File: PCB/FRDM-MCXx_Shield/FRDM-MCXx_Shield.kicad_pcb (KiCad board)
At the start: 2 copper layers, 91.4 x 54.6 mm, 45 parts, among them J1 Conn_01x05_Socket, J3 Conn_01x04_Socket, M1 Motor_Servo, SW1 PEC11L-4120F-N0020, SW2 SW_Push, U1 STPIC6C595MTR, U2 SN74LV164ADR, U3 M95010-RMN6TP, U4 FXLS8974CF, U5 SHT31A-DIS

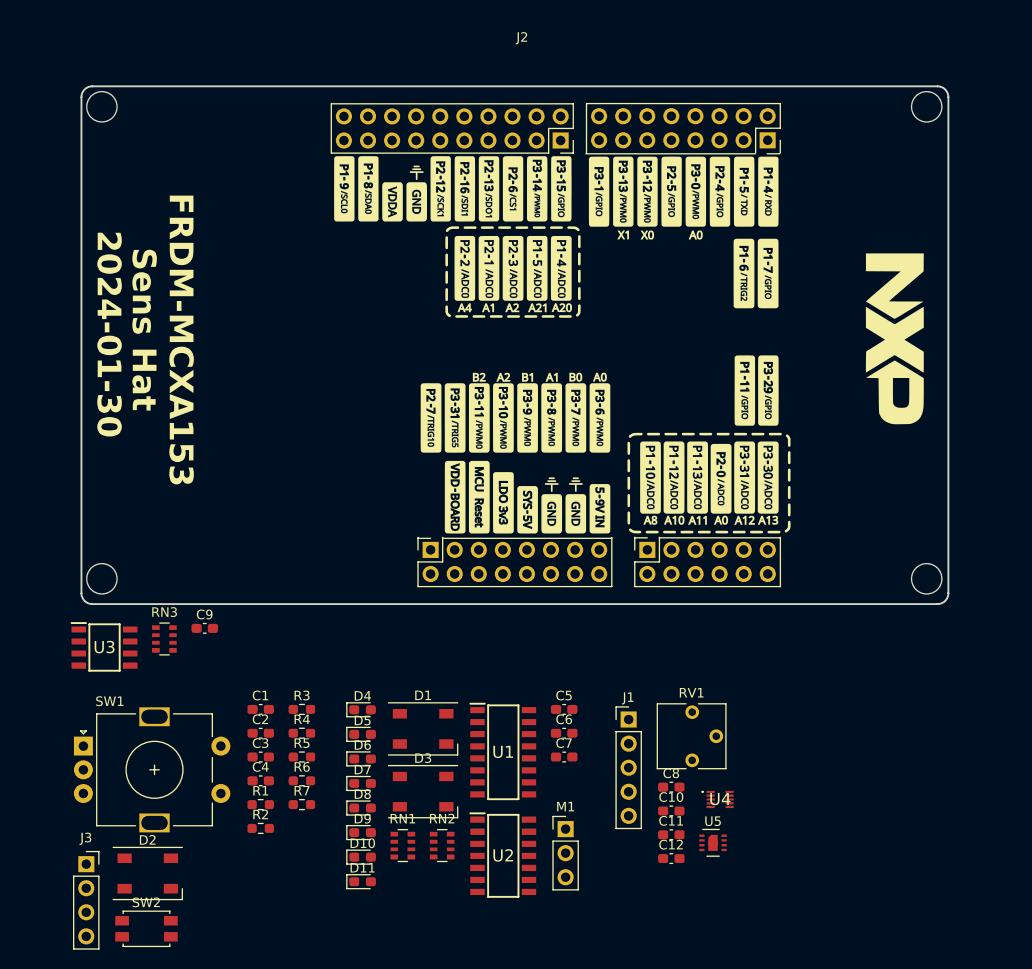
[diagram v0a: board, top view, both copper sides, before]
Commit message: Update schematic and footprint
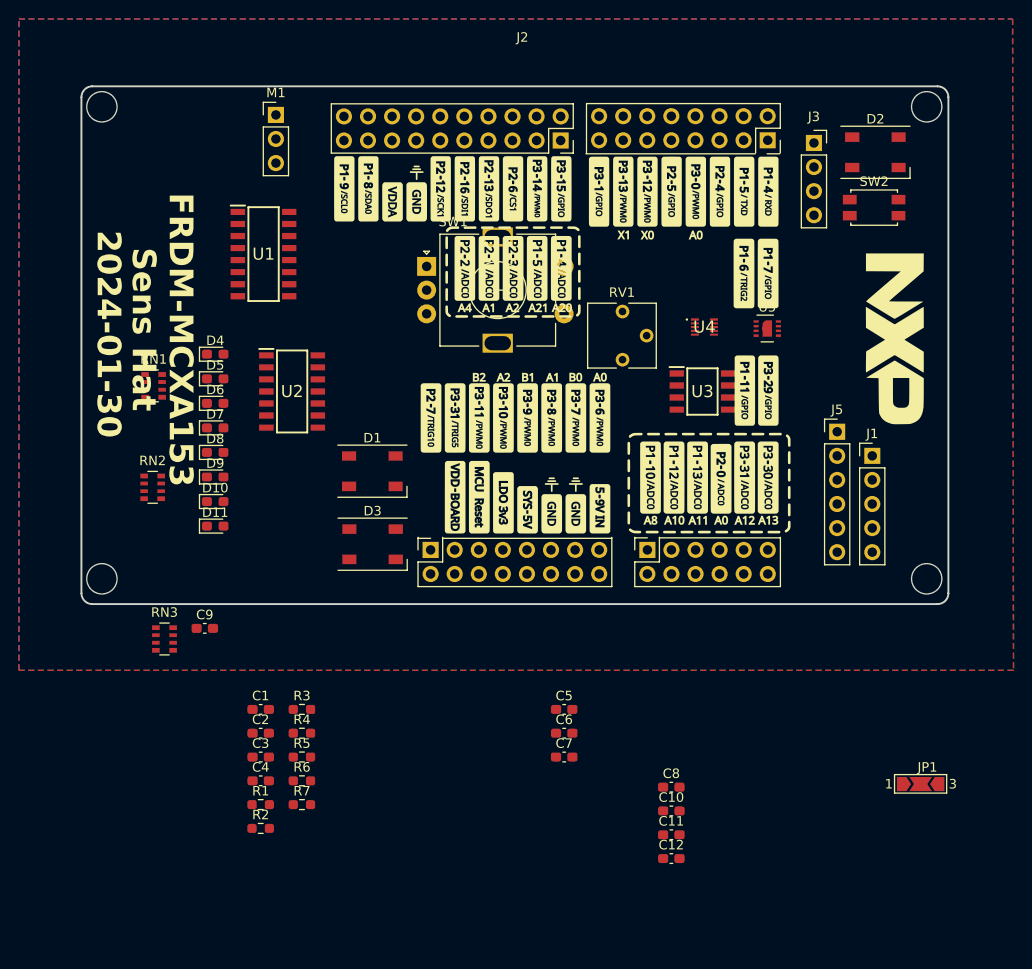
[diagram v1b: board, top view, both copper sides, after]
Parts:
- added J5: Conn_01x06_Socket, Connector_PinHeader_2.54mm:PinHeader_1x06_P2.54mm_Vertical, F.Cu at (183.9, 95.5)
- added JP1: SolderJumper_3_Open, Jumper:SolderJumper-3_P2.0mm_Open_TrianglePad1.0x1.5mm_NumberLabels, F.Cu at (192.7, 132.7)
- moved D2 108.1 mm to (187.9, 66.1)
- moved SW2 108.1 mm to (187.8, 71.9)
- moved J3 108.1 mm to (181.4, 65.1)
- moved M1 81.3 mm to (124.7, 62.1)
- moved U3 68.6 mm to (169.7, 91.3)
- moved SW1 62.2 mm to (140.6, 78.1)
- moved U1 58.3 mm to (123.4, 76.8)
- moved RN1 55.2 mm to (111.8, 90.7)
- moved U5 54.5 mm to (176.5, 84.7)
- moved U2 53.8 mm to (126.4, 91.3)
- moved U4 49.8 mm to (169.9, 84.5)
- moved RN2 48.6 mm to (111.7, 101.4)
- moved RV1 42.9 mm to (161.3, 87.9)
- moved D11 40.6 mm to (118.3, 105.5)
- moved D10 40.6 mm to (118.3, 102.9)
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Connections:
- net /Actuators/LED_NEOPIXEL renamed /LED_NEOPIXEL
- net /Actuators/~{SPI_CS} renamed /~{SPI_CS}
- net /HMI/ENC_SW renamed /ENC_SW
- net /HMI/LED_B renamed /LED_B
- net /HMI/LED_G renamed /LED_G
- net /HMI/LED_R renamed /LED_R
- net /Sensors/ACEL_INT1 renamed /ACEL_INT1
- net /Sensors/GPS_PPS renamed /GPS_PPS
- C8 pad 1: +3.3V -> Net-(JP1-C)
- J1 pad 3: /Sensors/GPS_TX -> /RX
- J1 pad 4: /Sensors/GPS_RX -> /TX
- J2 pad 1: unconnected-(J2-Pad1) -> /ENC_B
- J2 pad 10: unconnected-(J2A-SYS-5V-Pad10) -> +5V
- J2 pad 12: unconnected-(J2A-GND-Pad12) -> /ACEL_INT2
- J2 pad 14: unconnected-(J2A-GND-Pad14) -> /SERVO_PWM
- J2 pad 16: unconnected-(J2A-5-9VIN-Pad16) -> +3.3VADC
- J2 pad 18: unconnected-(J2B-P1-8/SDA0-Pad18) -> /SDA
- J2 pad 2: unconnected-(J2A-NC-Pad2) -> /ADC_OUT
- J2 pad 20: unconnected-(J2B-P1-9/SCL0-Pad20) -> /SCL
- J2 pad 3: unconnected-(J2-Pad3) -> /ENC_A
- J2 pad 4: unconnected-(J2A-VDD-BOARD-Pad4) -> +3.3V
- J2 pad 5: unconnected-(J2-Pad5) -> /SWITCH
- J2 pad 6: unconnected-(J2A-MCU-RESETb-Pad6) -> /ACEL_CS
- J2 pad 7: unconnected-(J2-Pad7) -> /~{TEMP_RST}
- J2 pad 8: unconnected-(J2A-LDO-3v3-Pad8) -> +3.3V
- J2 pad 9: unconnected-(J2-Pad9) -> /TEMP_ALERT
- J3 pad 1: /HMI/SDA -> /SDA
- J3 pad 2: /HMI/SCL -> /SCL
- M1 pad 1: /Actuators/SERVO_PWM -> /SERVO_PWM
- R1 pad 2: /HMI/SWITCH -> /SWITCH
- R3 pad 2: /HMI/ENC_A -> /ENC_A
- R4 pad 2: /HMI/ENC_B -> /ENC_B
- RN3 pad 2: /Sensors/ACEL_INT2 -> /ACEL_INT2
- RV1 pad 1: +3.3V -> Net-(JP1-C)
- RV1 pad 2: /Sensors/ADC_OUT -> /ADC_OUT
- U2 pad 1: /Actuators/SPI_MOSI -> /SPI_MOSI
- U2 pad 2: /Actuators/SPI_MOSI -> /SPI_MOSI
- U2 pad 8: /Actuators/SPI_CLK -> /SPI_CLK
- U4 pad 3: /Sensors/SPI_MISO -> /SPI_MISO
- U4 pad 4: /Sensors/SPI_MOSI -> /SPI_MOSI
- U4 pad 5: /Sensors/SPI_CLK -> /SPI_CLK
- U4 pad 6: /Sensors/ACEL_INT2 -> /ACEL_INT2
- U4 pad 7: /Sensors/ACEL_CS -> /ACEL_CS
- U5 pad 1: /Sensors/SDA -> /SCL
- U5 pad 3: /Sensors/TEMP_ALERT -> /TEMP_ALERT
- U5 pad 4: /Sensors/SCL -> /SDA
- U5 pad 6: /Sensors/~{TEMP_RST} -> /~{TEMP_RST}
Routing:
- added copper zone on B.Cu, net GND
- added copper zone on F.Cu, net GND

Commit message: Updated schematic and PCB
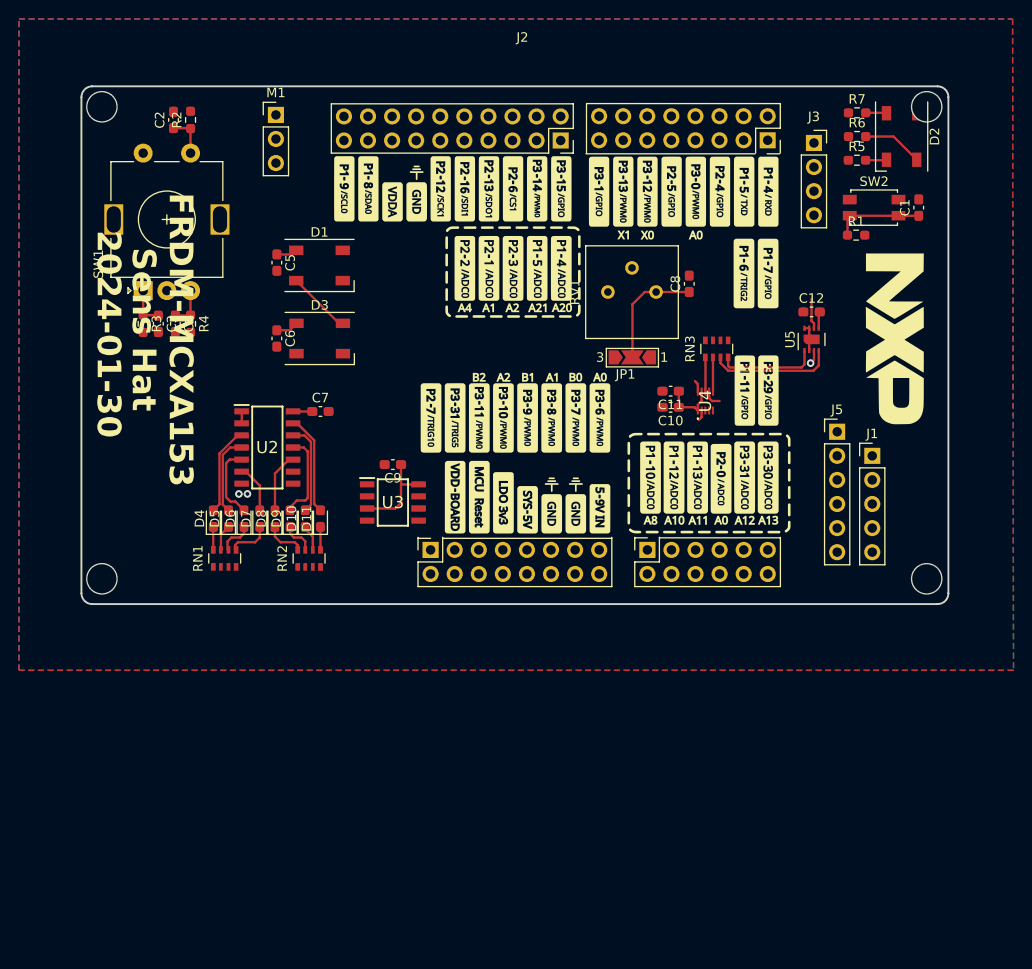
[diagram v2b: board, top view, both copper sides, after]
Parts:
- removed U1: STPIC6C595MTR, SamacSys_Parts:SOIC127P600X175-16N
- RV1: footprint Potentiometer_THT:Potentiometer_Vishay_T73YP_Vertical -> Potentiometer_THT:Potentiometer_Bourns_3386P_Vertical
- moved R7 93.6 mm to (186.0, 61.9)
- moved R6 89.7 mm to (186.0, 64.4)
- moved C1 87.3 mm to (192.5, 71.9), turned to 90 degrees
- moved R1 86.9 mm to (185.9, 74.8)
- moved R5 86.0 mm to (186.0, 66.9)
- moved R2 75.1 mm to (115.7, 62.6), turned to 90 degrees
- moved RN3 65.8 mm to (171.2, 86.8), turned to 90 degrees
- moved C2 65.3 mm to (113.9, 62.6), turned to 90 degrees
- moved C12 59.5 mm to (181.2, 82.9)
- moved C5 56.0 mm to (124.8, 77.7), turned to -90 degrees
- moved JP1 54.3 mm to (162.3, 87.7), turned to 180 degrees
- moved C8 53.1 mm to (168.3, 79.9), turned to 90 degrees
- moved C6 51.5 mm to (124.8, 85.7), turned to -90 degrees
- moved C4 49.0 mm to (114.1, 84.2), turned to -90 degrees
- moved C3 47.0 mm to (112.3, 84.2), turned to -90 degrees
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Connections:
- RN3 pad 3: /SCL -> /SDA
- RN3 pad 4: /SDA -> /SCL
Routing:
- net +3.3V: track 0.00 -> 24.3 mm
- net /SDA: track 0.00 -> 13.1 mm
- net Net-(JP1-C): track 0.00 -> 12.1 mm
- net /Actuators/LED_H: track 0.00 -> 10.6 mm
- net /SCL: track 0.00 -> 10.6 mm
- net /Actuators/LED_G: track 0.00 -> 9.64 mm
- net Net-(C1-Pad1): track 0.00 -> 9.43 mm
- net /Actuators/LED_A: track 0.00 -> 9.39 mm
- net /Actuators/LED_F: track 0.00 -> 9.22 mm
- net /Actuators/LED_B: track 0.00 -> 8.41 mm
- net /Actuators/LED_C: track 0.00 -> 7.85 mm
- net Net-(D1-DOUT): track 0.00 -> 6.79 mm
- net /Actuators/LED_E: track 0.00 -> 6.40 mm
- net Net-(D2-GK): track 0.00 -> 6.40 mm
- net GND: track 0.00 -> 5.41 mm, vias 0 -> 2
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
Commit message: Updated schematic and PCB files
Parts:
- added D1: RED, LED_SMD:LED_0603_1608Metric_Pad1.05x0.95mm_HandSolder, F.Cu at (164.5, 92.5)
- added D2: GREEN, LED_SMD:LED_0603_1608Metric_Pad1.05x0.95mm_HandSolder, F.Cu at (164.5, 94.4)
- added D3: BZV55B9V1, Diode_SMD:D_SOD-128, F.Cu at (108.3, 92.2)
- added F1: 300mA, Fuse:Fuse_0603_1608Metric_Pad1.05x0.95mm_HandSolder, F.Cu at (116.2, 93.0)
- added H1: MountingHole, MountingHole:MountingHole_2.5mm, F.Cu at (192.3, 103.1)
- added J2: Barrel_Jack_Switch, Connector_BarrelJack:BarrelJack_Wuerth_6941xx301002, F.Cu at (114.5, 100.7)
- added Q1: IRLML6401, Package_TO_SOT_SMD:SOT-23, F.Cu at (112.5, 92.2)
- added R1: 330, Resistor_SMD:R_0603_1608Metric_Pad0.98x0.95mm_HandSolder, F.Cu at (167.9, 92.5)
- added R2: 470, Resistor_SMD:R_0603_1608Metric_Pad0.98x0.95mm_HandSolder, F.Cu at (167.9, 94.4)
- added R3: 100k, Resistor_SMD:R_0603_1608Metric_Pad0.98x0.95mm_HandSolder, F.Cu at (112.5, 89.0)
- J4: renamed from J1; footprint Connector_PinHeader_2.54mm:PinHeader_1x05_P2.54mm_Vertical -> Connector_PinSocket_2.54mm:PinSocket_1x05_P2.54mm_Vertical
- J5: footprint Connector_PinHeader_2.54mm:PinHeader_1x06_P2.54mm_Vertical -> Connector_PinSocket_2.54mm:PinSocket_1x06_P2.54mm_Vertical
- moved C9 38.9 mm to (142.4, 86.2), turned to 90 degrees
- moved U3 35.9 mm to (145.3, 86.2), turned to 180 degrees
- moved C6 32.9 mm to (135.3, 80.2)
- moved C7 32.9 mm to (135.3, 81.9)
- moved RN1 32.9 mm to (140.2, 75.7)
- moved U2 32.9 mm to (139.0, 81.2)
- moved J3 24.5 mm to (183.3, 89.5), turned to 180 degrees
- moved C8 13.4 mm to (156.0, 85.3), turned to -90 degrees
- moved JP1 10.2 mm to (162.0, 77.5), turned to 0 degrees
- moved RV1 6.45 mm to (159.5, 84.4), turned to -90 degrees
- moved R7 4.04 mm to (181.9, 75.3)
- moved R10 4.04 mm to (182.0, 62.4)
- moved C5 4.04 mm to (188.5, 72.4)
- moved D4 4.04 mm to (186.7, 64.9)
- moved R8 4.04 mm to (182.0, 67.4)
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- renumbered C9 to C1, C5 to C10, C6 to C11, C7 to C12, C1 to C5, C11 to C6, C10 to C7, C12 to C9, D7 to D10, D8 to D11, D9 to D12, D10 to D13, D11 to D14, D2 to D4, D1 to D5, D3 to D6, D4 to D7, D5 to D8, D6 to D9, J2 to J1, R7 to R10, R2 to R4, R3 to R5, R4 to R6, R1 to R7, R5 to R8, R6 to R9, RN3 to RN1, RN1 to RN2, RN2 to RN3, U3 to U1, U4 to U2, U5 to U3, U2 to U5
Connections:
- JP1 pad 1: +3.3V -> +3.3VADC
- JP1 pad 3: +3.3VADC -> +3.3V
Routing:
- net +3.3V: track 24.3 -> 316.2 mm, vias 0 -> 11
- net +5V: track 0.00 -> 148.5 mm, vias 0 -> 2
- net /SPI_MOSI: track 1.27 -> 109.5 mm, vias 0 -> 3
- net /SPI_CLK: track 0.00 -> 82.6 mm, vias 0 -> 5
- net /SCL: track 10.6 -> 87.0 mm, vias 0 -> 2
- net /~{SPI_CS}: track 0.00 -> 72.1 mm, vias 0 -> 2
- net VBUS: track 0.00 -> 71.0 mm, vias 0 -> 1
- net /SWITCH: track 0.00 -> 70.2 mm, vias 0 -> 1
- net /SDA: track 13.1 -> 82.4 mm, vias 0 -> 1
- net /~{EEPROM_CS}: track 0.00 -> 62.6 mm, vias 0 -> 3
- net /ENC_SW: track 0.00 -> 62.2 mm, vias 0 -> 1
- net /ACEL_INT2: track 3.60 -> 63.5 mm, vias 0 -> 1
- net /ACEL_INT1: track 3.60 -> 62.5 mm, vias 0 -> 1
- net /SPI_MISO: track 0.00 -> 57.1 mm, vias 0 -> 2
- net /ENC_A: track 0.00 -> 54.7 mm
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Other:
- copper layers 2 -> 4

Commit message: Updated PCB
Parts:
- added ?: , clipboard:5e83e988-b69c-43c0-b382-9b895c3e7185, F.Cu at (187.2, 91.1)
- added Brd1: SSD1306, OLED:128x64OLED, F.Cu at (182.7, 85.5)
- moved R7 11.4 mm to (189.8, 67.1), turned to -90 degrees
- moved J3 10.0 mm to (193.3, 89.5)
- moved SW2 9.54 mm to (192.7, 69.0), turned to -90 degrees
- moved R8 5.36 mm to (182.3, 62.1), turned to -90 degrees
- moved R10 5.31 mm to (187.3, 62.1), turned to -90 degrees
- moved C5 4.39 mm to (192.7, 73.7), turned to 0 degrees
- moved R9 3.99 mm to (184.8, 62.1), turned to -90 degrees
- moved D4 2.66 mm to (184.8, 66.8), turned to 180 degrees
- moved J4 2.26 mm to (183.9, 100.3)
- moved J5 2.26 mm to (187.6, 97.8)
- moved M1 0.18 mm to (124.7, 62.3)
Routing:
- net +5V: track 148.5 -> 169.1 mm
- net /SDA: track 82.4 -> 95.6 mm
- net /SWITCH: track 70.2 -> 82.7 mm
- net /SCL: track 87.0 -> 99.4 mm
- net /LED_B: track 17.5 -> 23.7 mm
- net /LED_R: track 16.3 -> 12.6 mm
- net /TX: track 54.4 -> 56.7 mm
- net /RX: track 51.7 -> 53.9 mm
- net /GPS_PPS: track 17.8 -> 15.8 mm
- net /LED_G: track 16.8 -> 18.3 mm
- net +3.3V: track 316.2 -> 317.1 mm
- net /BT_EN: track 38.8 -> 37.9 mm
- added copper zone on In1.Cu, net GND
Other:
- board text added: "FRDM-MCXA153 Sens Hat 2024-01-30"

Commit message: Updated PCB
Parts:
- removed Brd1: SSD1306, OLED:128x64OLED
- added G***: LOGO, User:HAN_logo, F.Cu at (135.8, 93.9)
- added kibuzzard-65C7C452: G***, kibuzzard-65C7C452, F.Cu at (121.5, 62.3)
- added kibuzzard-65C7C4BF: G***, kibuzzard-65C7C4BF, F.Cu at (180.7, 105.5)
- added kibuzzard-65C7C4D7: G***, kibuzzard-65C7C4D7, F.Cu at (180.7, 108.0)
- added kibuzzard-65C7C4F7: G***, kibuzzard-65C7C4F7, F.Cu at (191.3, 110.4)
- added kibuzzard-65C7C50F: G***, kibuzzard-65C7C50F, F.Cu at (180.7, 110.5)
- added kibuzzard-65C7C529: G***, kibuzzard-65C7C529, F.Cu at (190.7, 108.0)
- added kibuzzard-65C7C54F: G***, kibuzzard-65C7C54F, F.Cu at (190.7, 105.4)
- added kibuzzard-65C7C588: G***, kibuzzard-65C7C588, F.Cu at (190.7, 100.4)
- added kibuzzard-65C7C594: G***, kibuzzard-65C7C594, F.Cu at (190.7, 102.9)
- added kibuzzard-65C7C5A7: G***, kibuzzard-65C7C5A7, F.Cu at (190.1, 81.9)
- added kibuzzard-65C7C5A7: G***, kibuzzard-65C7C5A7, F.Cu at (180.7, 102.9)
- added kibuzzard-65C7C5B4: G***, kibuzzard-65C7C5B4, F.Cu at (180.7, 100.3)
- added kibuzzard-65C7C5C0: G***, kibuzzard-65C7C5C0, F.Cu at (121.5, 64.9)
- added kibuzzard-65C7C5CF: G***, kibuzzard-65C7C5CF, F.Cu at (121.5, 67.4)
- added kibuzzard-65C7C6A4: G***, kibuzzard-65C7C6A4, F.Cu at (161.4, 91.5)
- added kibuzzard-65C7C6B6: G***, kibuzzard-65C7C6B6, F.Cu at (161.4, 93.4)
- added kibuzzard-65C7C6CC: G***, kibuzzard-65C7C6CC, F.Cu at (190.7, 97.8)
- added kibuzzard-65C7C73C: G***, kibuzzard-65C7C73C, F.Cu at (190.1, 84.4)
- added kibuzzard-65C7C751: G***, kibuzzard-65C7C751, F.Cu at (190.1, 87.0)
- added kibuzzard-65C7C77A: G***, kibuzzard-65C7C77A, F.Cu at (190.1, 89.6)
- added kibuzzard-65C7C9E9: G***, kibuzzard-65C7C9E9, F.Cu at (116.2, 100.5)
- added kibuzzard-65C7CAB6: G***, kibuzzard-65C7CAB6, F.Cu at (123.5, 102.2)
- added kibuzzard-65C7CB3C: G***, kibuzzard-65C7CB3C, F.Cu at (135.6, 106.7)
- added kibuzzard-65C7CC57: G***, kibuzzard-65C7CC57, F.Cu at (186.0, 112.7)
- added kibuzzard-65C7CCAF: G***, kibuzzard-65C7CCAF, F.Cu at (140.9, 81.2)
- added kibuzzard-65C7CCCF: G***, kibuzzard-65C7CCCF, F.Cu at (147.7, 86.1)
- added kibuzzard-65C7CD45: G***, kibuzzard-65C7CD45, F.Cu at (167.6, 84.2)
- added kibuzzard-65C7CD9F: G***, kibuzzard-65C7CD9F, F.Cu at (180.5, 68.6)
- added kibuzzard-65C7CE04: G***, kibuzzard-65C7CE04, F.Cu at (194.9, 68.8)
- added kibuzzard-65C7CE88: G***, kibuzzard-65C7CE88, F.Cu at (129.1, 74.8)
- added kibuzzard-65C7CF02: G***, kibuzzard-65C7CF02, F.Cu at (120.7, 73.2)
- added kibuzzard-65C7CF1C: G***, kibuzzard-65C7CF1C, F.Cu at (126.7, 64.7)
- added kibuzzard-65C7CF57: G***, kibuzzard-65C7CF57, F.Cu at (191.7, 79.8)
- added kibuzzard-65C7E4DC: G***, kibuzzard-65C7E4DC, B.Cu at (128.0, 103.6)
- moved RN2 2.00 mm to (119.3, 110.9)
- moved RN3 2.00 mm to (128.2, 110.9)
- moved D4 1.60 mm to (184.8, 68.4)
- moved R10 1.60 mm to (187.3, 63.7)
- moved R8 1.60 mm to (182.3, 63.7)
- moved R9 1.60 mm to (184.8, 63.7)
- moved ? 1.50 mm to (185.7, 91.1)
- moved D1 1.00 mm to (164.5, 91.5)
- moved D2 1.00 mm to (164.5, 93.4)
- moved R1 1.00 mm to (167.9, 91.5)
- moved R2 1.00 mm to (167.9, 93.4)
- moved R7 0.32 mm to (189.5, 67.1)
- moved C5 0.32 mm to (192.4, 73.7)
- moved SW2 0.32 mm to (192.4, 69.0)
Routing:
- net Net-(D14-K): track 2.42 -> 4.42 mm
- net Net-(D11-K): track 4.30 -> 6.30 mm
- net Net-(D8-K): track 2.76 -> 4.76 mm
- net Net-(D13-K): track 2.76 -> 4.76 mm
- net Net-(D7-K): track 2.47 -> 4.42 mm
- net Net-(D12-K): track 3.56 -> 5.44 mm
- net Net-(D10-K): track 4.56 -> 6.40 mm
- net Net-(D9-K): track 3.67 -> 5.51 mm
- net /LED_R: track 12.6 -> 14.2 mm
- net /LED_G: track 18.3 -> 19.9 mm
- net /LED_B: track 23.7 -> 25.3 mm
